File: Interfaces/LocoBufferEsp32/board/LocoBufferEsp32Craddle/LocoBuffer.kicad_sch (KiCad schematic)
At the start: 5 parts, among them U5 ESP32-DevKitC

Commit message: Correccion Pins
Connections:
- net LnRx: now also U5.36 (GPIO22); no longer U5.37 (GPIO23)
- net LnTx: now also U5.37 (GPIO23); no longer U5.36 (GPIO22)
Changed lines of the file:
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@@
     (stroke (width 0) (type default))
   )
-  (label "LnRx" (at 275.59 76.2 0) (fields_autoplaced)
+  (label "LnRx" (at 275.59 73.66 0) (fields_autoplaced)
     (effects (font (size 1.27 1.27)) (justify left bottom))
   )
@@
     (effects (font (size 1.27 1.27)) (justify left bottom))
   )
-  (label "LnTx" (at 275.59 73.66 0) (fields_autoplaced)
+  (label "LnTx" (at 275.59 76.2 0) (fields_autoplaced)
     (effects (font (size 1.27 1.27)) (justify left bottom))
   )
@@
   (symbol (lib_id "power:+3.3V") (at 236.22 40.64 0) (unit 1)
     (in_bom yes) (on_board yes) (dnp no)
-    (property "Reference" "#PWR018" (at 236.22 44.45 0)
-      (effects (font (size 1.27 1.27)) hide)
-    )
+    (property "Reference" "#PWR037" (at 236.22 44.45 0)
+      (effects (font (size 1.27 1.27)) hide)
+    )

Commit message: Mejoras Cradle
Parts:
- added J1: Conn_01x04, Connector_PinHeader_2.54mm:PinHeader_1x04_P2.54mm_Vertical, symbol Connector_Generic:Conn_01x04
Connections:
- net +3.3V: now also J1.2 (Pin_2)
- net GND: now also J1.1 (Pin_1)
- net SDA: now reaches U5.10 (DAC_2/ADC2_CH9/GPIO26)
- net SDA: now also J1.4 (Pin_4)
- net SCL: now reaches U5.11 (ADC2_CH7/GPIO27)
- net SCL: now also J1.3 (Pin_3)
- no-connect marks 30 -> 28
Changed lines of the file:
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@@
   (no_connect (at 266.7 48.26))
   (no_connect (at 200.66 73.66))
-  (no_connect (at 266.7 81.28))
   (no_connect (at 266.7 106.68))
   (no_connect (at 266.7 101.6))
@@
   (no_connect (at 200.66 66.04))
   (no_connect (at 266.7 60.96))
-  (no_connect (at 266.7 83.82))
   (no_connect (at 266.7 109.22))
   (no_connect (at 200.66 48.26))
+  (wire (pts (xy 109.22 82.55) (xy 109.22 81.28))
+    (stroke (width 0) (type default))
+  )
   (wire (pts (xy 161.29 24.13) (xy 157.48 24.13))
     (stroke (width 0) (type default))
@@
     (stroke (width 0) (type default))
   )
+  (wire (pts (xy 129.54 80.01) (xy 133.35 80.01))
+    (stroke (width 0) (type default))
+  )
   (wire (pts (xy 157.48 21.59) (xy 161.29 21.59))
     (stroke (width 0) (type default))
   )
+  (wire (pts (xy 114.3 77.47) (xy 133.35 77.47))
+    (stroke (width 0) (type default))
+  )
+  (wire (pts (xy 129.54 82.55) (xy 133.35 82.55))
+    (stroke (width 0) (type default))
+  )
   (wire (pts (xy 229.87 41.91) (xy 233.68 41.91))
     (stroke (width 0) (type default))
@@
     (stroke (width 0) (type default))
   )
+  (wire (pts (xy 100.33 78.74) (xy 100.33 74.93))
+    (stroke (width 0) (type default))
+  )
   (wire (pts (xy 233.68 41.91) (xy 233.68 43.18))
     (stroke (width 0) (type default))
   )
+  (wire (pts (xy 266.7 83.82) (xy 271.78 83.82))
+    (stroke (width 0) (type default))
+  )
   (wire (pts (xy 266.7 76.2) (xy 275.59 76.2))
     (stroke (width 0) (type default))
   )
+  (wire (pts (xy 114.3 82.55) (xy 114.3 77.47))
+    (stroke (width 0) (type default))
+  )
+  (wire (pts (xy 266.7 81.28) (xy 271.78 81.28))
+    (stroke (width 0) (type default))
+  )
   (wire (pts (xy 236.22 40.64) (xy 236.22 43.18))
     (stroke (width 0) (type default))
@@
     (stroke (width 0) (type default))
   )
+  (wire (pts (xy 100.33 74.93) (xy 133.35 74.93))
+    (stroke (width 0) (type default))
+  )
+  (wire (pts (xy 109.22 82.55) (xy 114.3 82.55))
+    (stroke (width 0) (type default))
+  )
   (label "LnRx" (at 275.59 73.66 0) (fields_autoplaced)
     (effects (font (size 1.27 1.27)) (justify left bottom))
   )
+  (label "SCL" (at 129.54 80.01 180) (fields_autoplaced)
+    (effects (font (size 1.27 1.27)) (justify right bottom))
+  )
   (label "LnRx" (at 161.29 24.13 0) (fields_autoplaced)
     (effects (font (size 1.27 1.27)) (justify left bottom))
   )
+  (label "SCL" (at 271.78 83.82 0) (fields_autoplaced)
+    (effects (font (size 1.27 1.27)) (justify left bottom))
+  )
   (label "LnTx" (at 275.59 76.2 0) (fields_autoplaced)
     (effects (font (size 1.27 1.27)) (justify left bottom))
   )
+  (label "SDA" (at 271.78 81.28 0) (fields_autoplaced)
+    (effects (font (size 1.27 1.27)) (justify left bottom))
+  )
+  (label "SDA" (at 129.54 82.55 180) (fields_autoplaced)
+    (effects (font (size 1.27 1.27)) (justify right bottom))
+  )
   (label "LnTx" (at 161.29 21.59 0) (fields_autoplaced)
     (effects (font (size 1.27 1.27)) (justify left bottom))
@@
     )
   )
+  (symbol (lib_id "Connector_Generic:Conn_01x04") (at 138.43 77.47 0) (unit 1)
+    (in_bom yes) (on_board yes) (dnp no) (fields_autoplaced)
+    (property "Reference" "J1" (at 140.97 77.47 0)
+      (effects (font (size 1.27 1.27)) (justify left))
+    )
+    (property "Value" "Conn_01x04" (at 140.97 80.01 0)
+      (effects (font (size 1.27 1.27)) (justify left))
+    )
+    (property "Footprint" "Connector_PinHeader_2.54mm:PinHeader_1x04_P2.54mm_Vertical" (at 138.43 77.47 0)
+      (effects (font (size 1.27 1.27)))
+    )
+    (property "Datasheet" "~" (at 138.43 77.47 0)
+      (effects (font (size 1.27 1.27)) hide)
+    )
+    (pin "1")
+    (pin "2")
+    (pin "3")
+    (pin "4")
+    (instances
+      (project "LocoBuffer"
+        (path "/f41e9384-dd4d-4b6d-95c2-0d2355bf925d"
+          (reference "J1") (unit 1)
+        )
+      )
+    )
+  )
+  (symbol (lib_id "power:GND") (at 100.33 78.74 0) (unit 1)
+    (in_bom yes) (on_board yes) (dnp no)
+    (property "Reference" "#PWR015" (at 100.33 85.09 0)
+      (effects (font (size 1.27 1.27)) hide)
+    )
+    (property "Value" "GND" (at 100.457 83.1342 0)
+      (effects (font (size 1.27 1.27)))
+    )
+    (property "Footprint" "" (at 100.33 78.74 0)
+      (effects (font (size 1.27 1.27)) hide)
+    )
+    (property "Datasheet" "" (at 100.33 78.74 0)
+      (effects (font (size 1.27 1.27)) hide)
+    )
+    (pin "1")
+    (instances
+      (project "LocoBuffer"
+        (path "/f41e9384-dd4d-4b6d-95c2-0d2355bf925d"
+          (reference "#PWR015") (unit 1)
+        )
+      )
+    )
+  )
   (symbol (lib_id "power:+3.3V") (at 236.22 40.64 0) (unit 1)
     (in_bom yes) (on_board yes) (dnp no)
@@
         )
       )
+    )
+  )
+  (symbol (lib_id "power:+3.3V") (at 109.22 81.28 0) (unit 1)
+    (in_bom yes) (on_board yes) (dnp no)
+    (property "Reference" "#PWR016" (at 109.22 85.09 0)
+      (effects (font (size 1.27 1.27)) hide)
+    )
+    (property "Value" "+3.3V" (at 109.22 76.2 0)
+      (effects (font (size 1.27 1.27)))
+    )
+    (property "Footprint" "" (at 109.22 81.28 0)
+      (effects (font (size 1.27 1.27)) hide)
+    )
+    (property "Datasheet" "" (at 109.22 81.28 0)
+      (effects (font (size 1.27 1.27)) hide)
+    )
+    (pin "1")
+    (instances
+      (project "LocoBuffer"
+        (path "/f41e9384-dd4d-4b6d-95c2-0d2355bf925d"
+          (reference "#PWR016") (unit 1)
+        )
+      )

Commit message: LocoCradle
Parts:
- added C1, C2: 22 uF, Capacitor_SMD:C_1206_3216Metric, symbol Device:C
- added D1 (x2): LED, LED_SMD:LED_0805_2012Metric, symbol Device:LED
- added D3, D4, D5: SS24A, Diode_SMD:D_SMA, symbol Device:D
- added R6 (x2): 470, Resistor_SMD:R_0805_2012Metric, symbol Device:R
- added U2: AMS1117-5.0, Package_TO_SOT_SMD:SOT-223-3_TabPin2, symbol Regulator_Linear:AMS1117-5.0
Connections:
- net +3.3V: now also R6.2
- net +5V: now also D5.1 (K)
- net GND: now also C1.2, C2.2, D1.1 (K), D1.1 (K), U2.1 (GND)
- new net: D1.2 (A), R6.1 (x2)
- new net LnPower: C2.1, D3.1 (K), D4.1 (K), U2.3 (VI)
- new net LnPower5V: C1.1, D5.2 (A), R6.2, U2.2 (VO)
- new net LocoNet/RSyncA: D3.2 (A)
- new net LocoNet/RSyncB: D4.2 (A)
- no-connect marks 28 -> 29
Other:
- sheet LocoNet ports: added RSyncA, RSyncB; removed none
- moved on the sheet: J1, U5

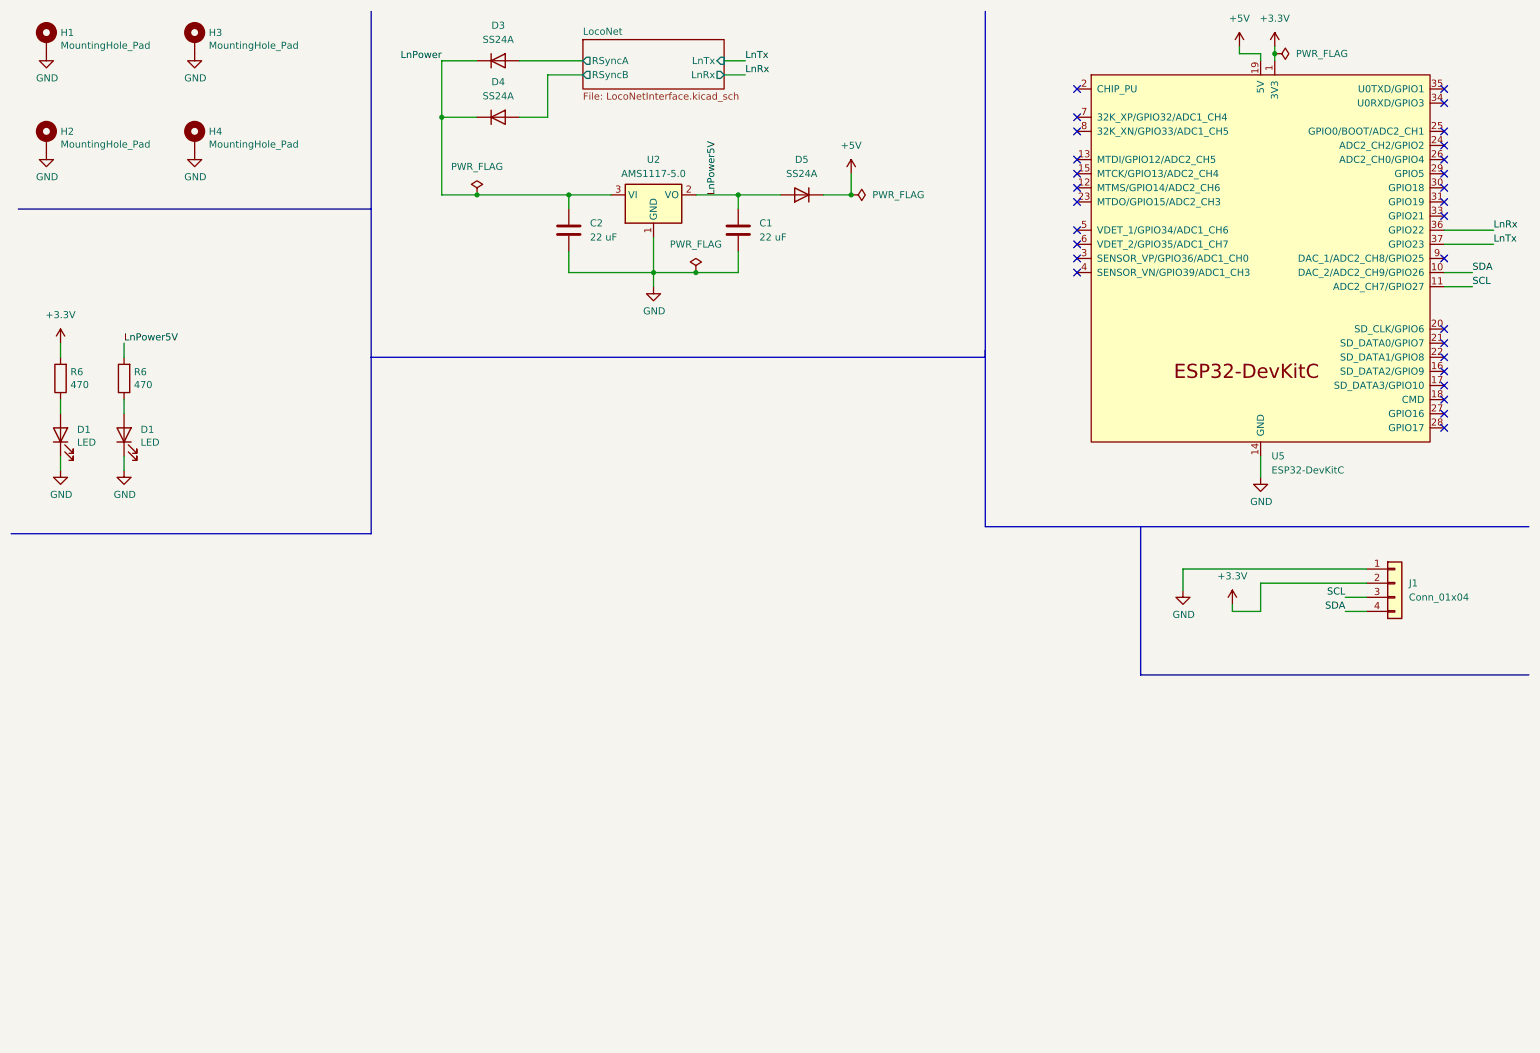
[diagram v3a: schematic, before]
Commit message: Btn and RGB Led
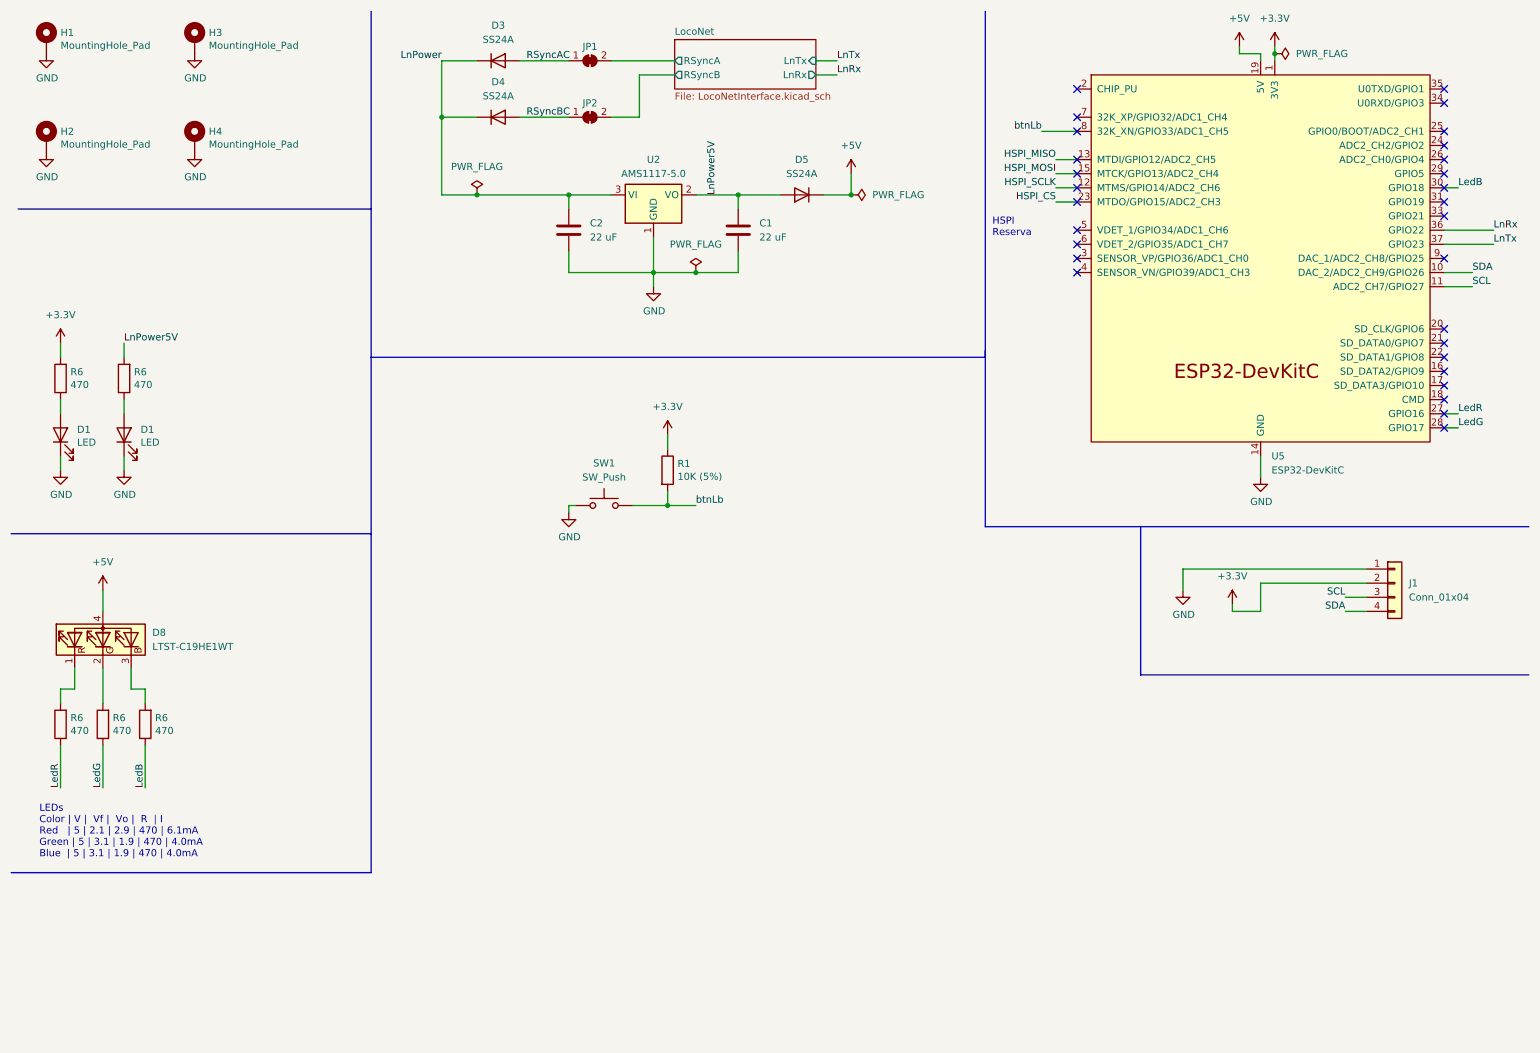
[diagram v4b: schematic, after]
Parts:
- added D8: LTST-C19HE1WT, LED_SMD:LED_LiteOn_LTST-C19HE1WT, symbol Device:LED_RGBA
- added JP1, JP2: SolderJumper_2_Bridged, Jumper:SolderJumper-2_P1.3mm_Bridged2Bar_RoundedPad1.0x1.5mm, symbol Jumper:SolderJumper_2_Bridged
- added R1: 10K (5%), Resistor_SMD:R_0805_2012Metric, symbol Device:R
- added R6 (x3): 470, Resistor_SMD:R_0805_2012Metric, symbol Device:R
- added SW1: SW_Push, Button_Switch_SMD:SW_SPST_CK_RS282G05A3, symbol Switch:SW_Push
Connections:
- net +3.3V: now also R1.1
- net +5V: now also D8.4 (A)
- net GND: now also SW1.1
- net LocoNet/RSyncA: now also JP1.2 (B); no longer D3.2 (A)
- net LocoNet/RSyncB: now also JP2.2 (B); no longer D4.2 (A)
- net HSPI_SCLK: now reaches U5.12 (MTMS/GPIO14/ADC2_CH6)
- net HSPI_MISO: now reaches U5.13 (MTDI/GPIO12/ADC2_CH5)
- net HSPI_MOSI: now reaches U5.15 (MTCK/GPIO13/ADC2_CH4)
- net HSPI_CS: now reaches U5.23 (MTDO/GPIO15/ADC2_CH3)
- net LedR: now reaches U5.27 (GPIO16)
- net LedR: now also R6.1
- net LedG: now reaches U5.28 (GPIO17)
- net LedG: now also R6.1
- net LedB: now reaches U5.30 (GPIO18)
- net LedB: now also R6.1
- net btnLb: now reaches U5.8 (32K_XN/GPIO33/ADC1_CH5)
- net btnLb: now also R1.2, SW1.2
- new net: D8.1 (RK), R6.2
- new net: D8.2 (GK), R6.2
- new net: D8.3 (BK), R6.2
- new net RSyncAC: D3.2 (A), JP1.1 (A)
- new net RSyncBC: D4.2 (A), JP2.1 (A)
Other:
- note added: "HSPI Reserva"
- note added: "LEDs Color | V | Vf | Vo | R | I Red | 5 | 2.1 | 2.9 | 470 | 6.1mA Green | 5 | 3.1 | 1.9 | 470 | 4.0mA Blue | 5 | 3.1 | 1.9 | 470 | 4.0mA"

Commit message: CleanUp
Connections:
- no-connect marks 29 -> 25
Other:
- company: (none) -> Dcc Diy Tools
- title: (none) -> LocoBuffer Esp32
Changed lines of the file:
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@@
 (kicad_sch (version 20230121) (generator eeschema)
   (paper "A4")
+  (title_block
+    (title "LocoBuffer Esp32")
+    (date "2023-07-17")
+    (rev "0.0.1")
+    (company "Dcc Diy Tools")
+  )
   (junction (at 142.24 45.72) (diameter 0) (color 0 0 0 0)
   )
@@
   (no_connect (at 269.24 26.67))
   (no_connect (at 203.2 52.07))
-  (no_connect (at 269.24 85.09))
-  (no_connect (at 203.2 34.29))
   (no_connect (at 269.24 80.01))
   (no_connect (at 203.2 54.61))
-  (no_connect (at 269.24 44.45))
   (no_connect (at 269.24 29.21))
   (no_connect (at 203.2 39.37))
@@
   (no_connect (at 203.2 44.45))
   (no_connect (at 269.24 39.37))
-  (no_connect (at 269.24 87.63))
   (no_connect (at 203.2 26.67))
   (wire (pts (xy 231.14 120.65) (xy 231.14 119.38))
@@
     (stroke (width 0) (type default))
   )
+  (wire (pts (xy 269.24 44.45) (xy 271.78 44.45))
+    (stroke (width 0) (type default))
+  )
   (wire (pts (xy 88.9 31.75) (xy 88.9 45.72))
     (stroke (width 0) (type default))
@@
     (stroke (width 0) (type default))
   )
-  (wire (pts (xy 269.24 44.45) (xy 271.78 44.45))
-    (stroke (width 0) (type default))
-  )
   (polyline (pts (xy 186.69 12.7) (xy 186.69 105.41))
     (stroke (width 0) (type default))
@@
     (stroke (width 0) (type default))
   )
+  (wire (pts (xy 196.85 34.29) (xy 203.2 34.29))
+    (stroke (width 0) (type default))
+  )
   (wire (pts (xy 31.75 82.55) (xy 31.75 85.09))
     (stroke (width 0) (type default))
@@
     (stroke (width 0) (type default))
   )
+  (wire (pts (xy 269.24 85.09) (xy 271.78 85.09))
+    (stroke (width 0) (type default))
+  )
   (wire (pts (xy 127 59.69) (xy 127 62.23))
     (stroke (width 0) (type default))
@@
     (stroke (width 0) (type default))
   )
+  (wire (pts (xy 269.24 87.63) (xy 271.78 87.63))
+    (stroke (width 0) (type default))
+  )
   (wire (pts (xy 111.76 101.6) (xy 113.03 101.6))
     (stroke (width 0) (type default))
@@
     (stroke (width 0) (type default))
   )
-  (wire (pts (xy 269.24 87.63) (xy 271.78 87.63))
-    (stroke (width 0) (type default))
-  )
   (wire (pts (xy 111.76 59.69) (xy 111.76 55.88))
     (stroke (width 0) (type default))
@@
     (stroke (width 0) (type default))
   )
-  (wire (pts (xy 196.85 34.29) (xy 203.2 34.29))
-    (stroke (width 0) (type default))
-  )
   (wire (pts (xy 102.87 31.75) (xy 111.76 31.75))
     (stroke (width 0) (type default))
   )
-  (wire (pts (xy 269.24 85.09) (xy 271.78 85.09))
-    (stroke (width 0) (type default))
-  )
